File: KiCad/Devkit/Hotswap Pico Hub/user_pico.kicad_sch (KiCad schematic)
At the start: 3 parts, among them J303 User SWD In, U1 User Pico

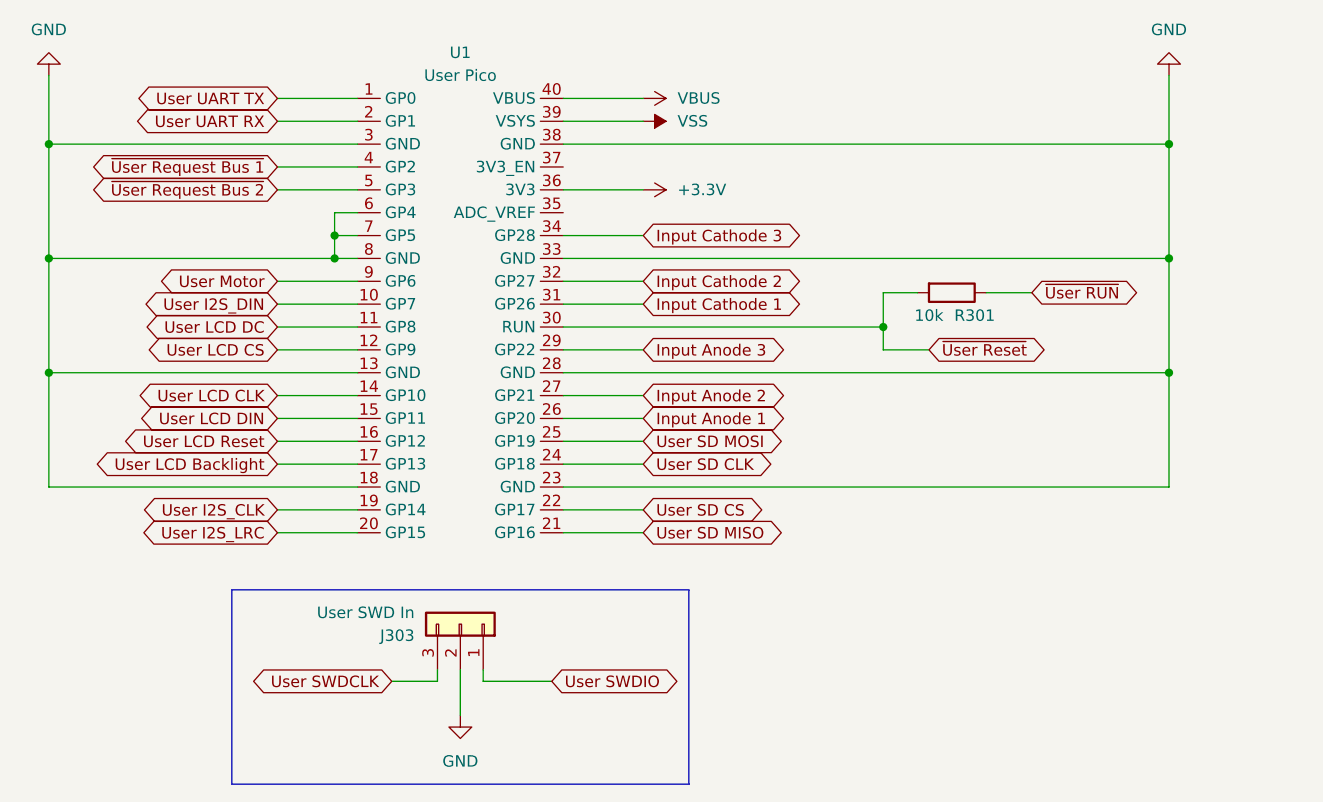
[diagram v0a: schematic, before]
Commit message: Updated KiCad to V1.1.2
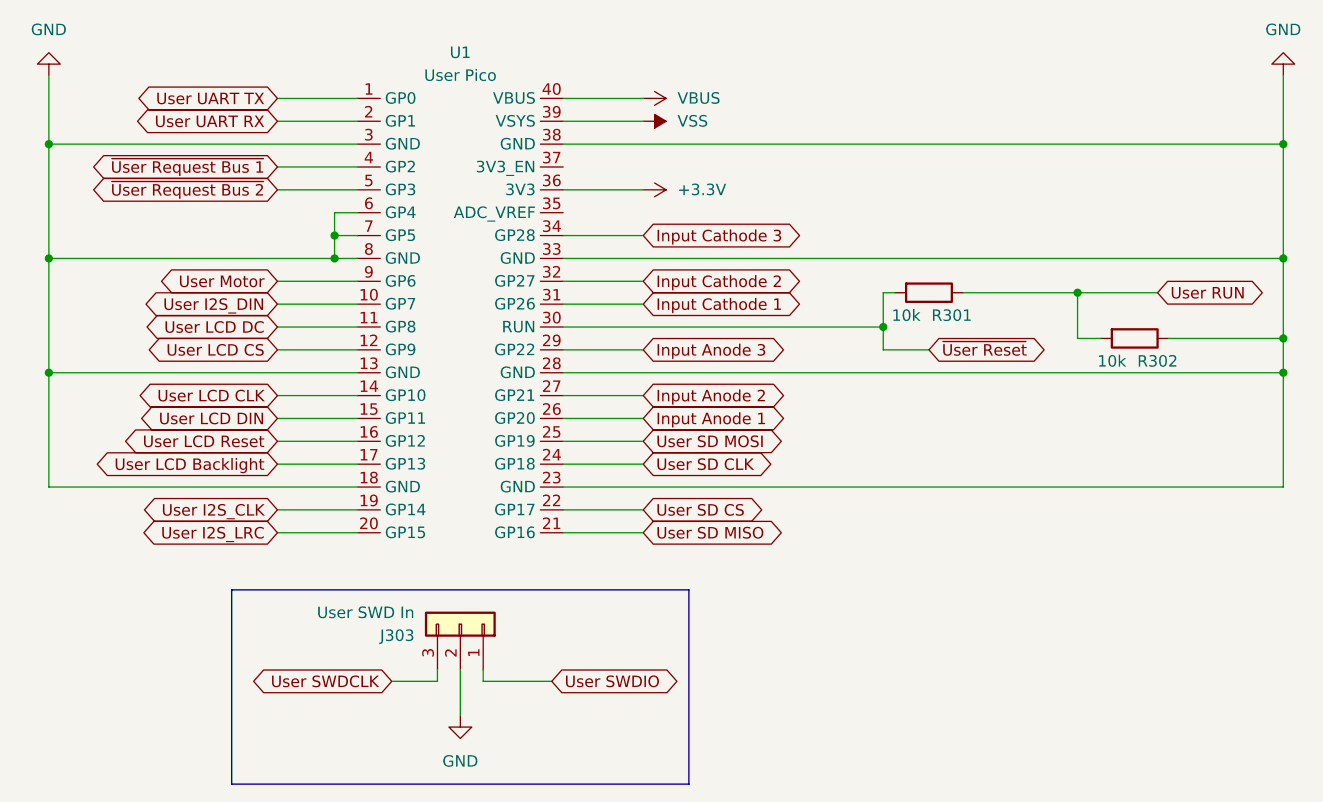
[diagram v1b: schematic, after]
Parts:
- added R302: 10k, Resistor_SMD:R_0805_2012Metric, symbol Device:R
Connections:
- net GND: now also R302.1
- net ~{User RUN} renamed User RUN
- net User RUN: now also R302.2
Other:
- moved on the sheet: R301
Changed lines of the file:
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@@
 (kicad_sch (version 20230121) (generator eeschema)
   (paper "A4")
-  (junction (at 151.13 66.04) (diameter 0) (color 0 0 0 0)
-  )
   (junction (at 26.67 40.64) (diameter 0) (color 0 0 0 0)
   )
+  (junction (at 163.83 66.04) (diameter 0) (color 0 0 0 0)
+  )
+  (junction (at 163.83 40.64) (diameter 0) (color 0 0 0 0)
+  )
   (junction (at 26.67 53.34) (diameter 0) (color 0 0 0 0)
   )
   (junction (at 119.38 60.96) (diameter 0) (color 0 0 0 0)
   )
-  (junction (at 151.13 53.34) (diameter 0) (color 0 0 0 0)
+  (junction (at 140.97 57.15) (diameter 0) (color 0 0 0 0)
+  )
+  (junction (at 163.83 53.34) (diameter 0) (color 0 0 0 0)
   )
   (junction (at 58.42 53.34) (diameter 0) (color 0 0 0 0)
@@
   (junction (at 26.67 66.04) (diameter 0) (color 0 0 0 0)
   )
-  (junction (at 151.13 40.64) (diameter 0) (color 0 0 0 0)
+  (junction (at 163.83 62.23) (diameter 0) (color 0 0 0 0)
   )
   (junction (at 58.42 50.8) (diameter 0) (color 0 0 0 0)
@@
     (stroke (width 0) (type default))
   )
+  (wire (pts (xy 83.82 40.64) (xy 163.83 40.64))
+    (stroke (width 0) (type default))
+  )
   (wire (pts (xy 58.42 48.26) (xy 58.42 50.8))
     (stroke (width 0) (type default))
@@
     (stroke (width 0) (type default))
   )
+  (wire (pts (xy 140.97 57.15) (xy 149.86 57.15))
+    (stroke (width 0) (type default))
+  )
   (wire (pts (xy 82.55 100.33) (xy 74.93 100.33))
     (stroke (width 0) (type default))
@@
     (stroke (width 0) (type default))
   )
+  (wire (pts (xy 83.82 53.34) (xy 163.83 53.34))
+    (stroke (width 0) (type default))
+  )
   (wire (pts (xy 58.42 50.8) (xy 60.96 50.8))
     (stroke (width 0) (type default))
@@
     (stroke (width 0) (type default))
   )
-  (wire (pts (xy 123.19 57.15) (xy 119.38 57.15))
+  (wire (pts (xy 120.65 57.15) (xy 119.38 57.15))
+    (stroke (width 0) (type default))
+  )
+  (wire (pts (xy 83.82 66.04) (xy 163.83 66.04))
     (stroke (width 0) (type default))
   )
@@
     (stroke (width 0) (type default))
   )
-  (wire (pts (xy 151.13 66.04) (xy 151.13 53.34))
-    (stroke (width 0) (type default))
-  )
-  (wire (pts (xy 130.81 57.15) (xy 135.89 57.15))
+  (wire (pts (xy 163.83 66.04) (xy 163.83 62.23))
+    (stroke (width 0) (type default))
+  )
+  (wire (pts (xy 128.27 57.15) (xy 140.97 57.15))
     (stroke (width 0) (type default))
   )
@@
     (stroke (width 0) (type default))
   )
-  (wire (pts (xy 151.13 53.34) (xy 151.13 40.64))
+  (wire (pts (xy 163.83 53.34) (xy 163.83 40.64))
     (stroke (width 0) (type default))
   )
@@
     (stroke (width 0) (type default))
   )
-  (wire (pts (xy 83.82 66.04) (xy 151.13 66.04))
+  (wire (pts (xy 143.51 62.23) (xy 140.97 62.23))
     (stroke (width 0) (type default))
   )
@@
     (stroke (width 0) (type default))
   )
-  (wire (pts (xy 83.82 53.34) (xy 151.13 53.34))
-    (stroke (width 0) (type default))
-  )
   (wire (pts (xy 52.07 83.82) (xy 60.96 83.82))
     (stroke (width 0) (type default))
@@
     (stroke (width 0) (type default))
   )
+  (wire (pts (xy 163.83 62.23) (xy 163.83 53.34))
+    (stroke (width 0) (type default))
+  )
   (wire (pts (xy 83.82 45.72) (xy 92.71 45.72))
     (stroke (width 0) (type default))
   )
+  (wire (pts (xy 151.13 62.23) (xy 163.83 62.23))
+    (stroke (width 0) (type default))
+  )
   (wire (pts (xy 26.67 53.34) (xy 26.67 66.04))
     (stroke (width 0) (type default))
@@
     (stroke (width 0) (type default))
   )
-  (wire (pts (xy 151.13 78.74) (xy 151.13 66.04))
+  (wire (pts (xy 163.83 78.74) (xy 163.83 66.04))
     (stroke (width 0) (type default))
   )
@@
     (stroke (width 0) (type default))
   )
-  (wire (pts (xy 151.13 40.64) (xy 151.13 33.02))
+  (wire (pts (xy 163.83 40.64) (xy 163.83 33.02))
     (stroke (width 0) (type default))
   )
@@
     (stroke (width 0) (type default))
   )
-  (wire (pts (xy 83.82 40.64) (xy 151.13 40.64))
-    (stroke (width 0) (type default))
-  )
   (wire (pts (xy 52.07 73.66) (xy 60.96 73.66))
     (stroke (width 0) (type default))
   )
-  (wire (pts (xy 83.82 78.74) (xy 151.13 78.74))
+  (wire (pts (xy 83.82 78.74) (xy 163.83 78.74))
     (stroke (width 0) (type default))
   )
@@
   )
   (wire (pts (xy 69.85 100.33) (xy 69.85 99.06))
+    (stroke (width 0) (type default))
+  )
+  (wire (pts (xy 140.97 62.23) (xy 140.97 57.15))
     (stroke (width 0) (type default))
   )
@@
     )
   )
-  (global_label "~{User RUN}" (shape bidirectional) (at 135.89 57.15 0) (fields_autoplaced)
-    (effects (font (size 1.27 1.27)) (justify left))
-    (property "Intersheetrefs" "${INTERSHEET_REFS}" (at 135.89 57.15 0)
-      (effects (font (size 1.27 1.27)) hide)
+  (global_label "User RUN" (shape bidirectional) (at 149.86 57.15 0) (fields_autoplaced)
+    (effects (font (size 1.27 1.27)) (justify left))
+    (property "Intersheetrefs" "${INTERSHEET_REFS}" (at 163.0885 57.15 0)
+      (effects (font (size 1.27 1.27)) (justify left) hide)
     )
   )
@@
     )
   )
-  (symbol (lib_id "power:GND") (at 151.13 33.02 180) (unit 1)
+  (symbol (lib_id "power:GND") (at 163.83 33.02 180) (unit 1)
     (in_bom yes) (on_board yes) (dnp no)
-    (property "Reference" "#PWR0111" (at 151.13 26.67 0)
-      (effects (font (size 1.27 1.27)) hide)
-    )
-    (property "Value" "GND" (at 151.13 27.94 0)
-      (effects (font (size 1.27 1.27)))
-    )
-    (property "Footprint" "" (at 151.13 33.02 0)
-      (effects (font (size 1.27 1.27)) hide)
-    )
-    (property "Datasheet" "" (at 151.13 33.02 0)
+    (property "Reference" "#PWR0111" (at 163.83 26.67 0)
+      (effects (font (size 1.27 1.27)) hide)
+    )
+    (property "Value" "GND" (at 163.83 27.94 0)
+      (effects (font (size 1.27 1.27)))
+    )
+    (property "Footprint" "" (at 163.83 33.02 0)
+      (effects (font (size 1.27 1.27)) hide)
+    )
+    (property "Datasheet" "" (at 163.83 33.02 0)
       (effects (font (size 1.27 1.27)) hide)
     )
@@
     )
   )
-  (symbol (lib_id "Device:R") (at 127 57.15 270) (unit 1)
+  (symbol (lib_id "Device:R") (at 124.46 57.15 270) (unit 1)
     (in_bom yes) (on_board yes) (dnp no)
-    (property "Reference" "R301" (at 129.54 59.69 90)
-      (effects (font (size 1.27 1.27)))
-    )
-    (property "Value" "10k" (at 124.46 59.69 90)
-      (effects (font (size 1.27 1.27)))
-    )
-    (property "Footprint" "Resistor_SMD:R_0805_2012Metric" (at 127 55.372 90)
-      (effects (font (size 1.27 1.27)) hide)
-    )
-    (property "Datasheet" "~" (at 127 57.15 0)
+    (property "Reference" "R301" (at 127 59.69 90)
+      (effects (font (size 1.27 1.27)))
+    )
+    (property "Value" "10k" (at 121.92 59.69 90)
+      (effects (font (size 1.27 1.27)))
+    )
+    (property "Footprint" "Resistor_SMD:R_0805_2012Metric" (at 124.46 55.372 90)
+      (effects (font (size 1.27 1.27)) hide)
+    )
+    (property "Datasheet" "~" (at 124.46 57.15 0)
       (effects (font (size 1.27 1.27)) hide)
     )
@@
         )
       )
+    )
+  )
+  (symbol (lib_id "Device:R") (at 147.32 62.23 270) (unit 1)
+    (in_bom yes) (on_board yes) (dnp no)
+    (property "Reference" "R302" (at 149.86 64.77 90)
+      (effects (font (size 1.27 1.27)))
+    )
+    (property "Value" "10k" (at 144.78 64.77 90)
+      (effects (font (size 1.27 1.27)))
+    )
+    (property "Footprint" "Resistor_SMD:R_0805_2012Metric" (at 147.32 60.452 90)
+      (effects (font (size 1.27 1.27)) hide)
+    )
+    (property "Datasheet" "~" (at 147.32 62.23 0)
+      (effects (font (size 1.27 1.27)) hide)
+    )
+    (pin "1")
+    (pin "2")
+    (instances
+      (project "DevkitHotswapPicoHub"
+        (path "/9538e4ed-27e6-4c37-b989-9859dc0d49e8/0d723066-7df4-4ebf-991e-b2ac94b6ffc4"
+          (reference "R302") (unit 1)
+        )
+      )
